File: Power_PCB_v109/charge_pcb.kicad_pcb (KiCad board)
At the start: 2 copper layers, 128.1 x 64 mm, 79 parts, among them J1 Mow3, J10 Mot_Left, J11 DC/DC1, J12 DC/DC2, J2 Main_PCB1, J3 Mow2, J4 Battery, J5 Main_PCB2, J6 Power Switch, J7 Mow1, J8 Mot_Right, J9 Start, Q1 BC547C, Q2 IRF9540N, Q3 BC547C, Q4 IRF9540N, U1 INA226, U2 INA226, U3 INA Charge, U4 INA226, U5 INA226, U6 INA226

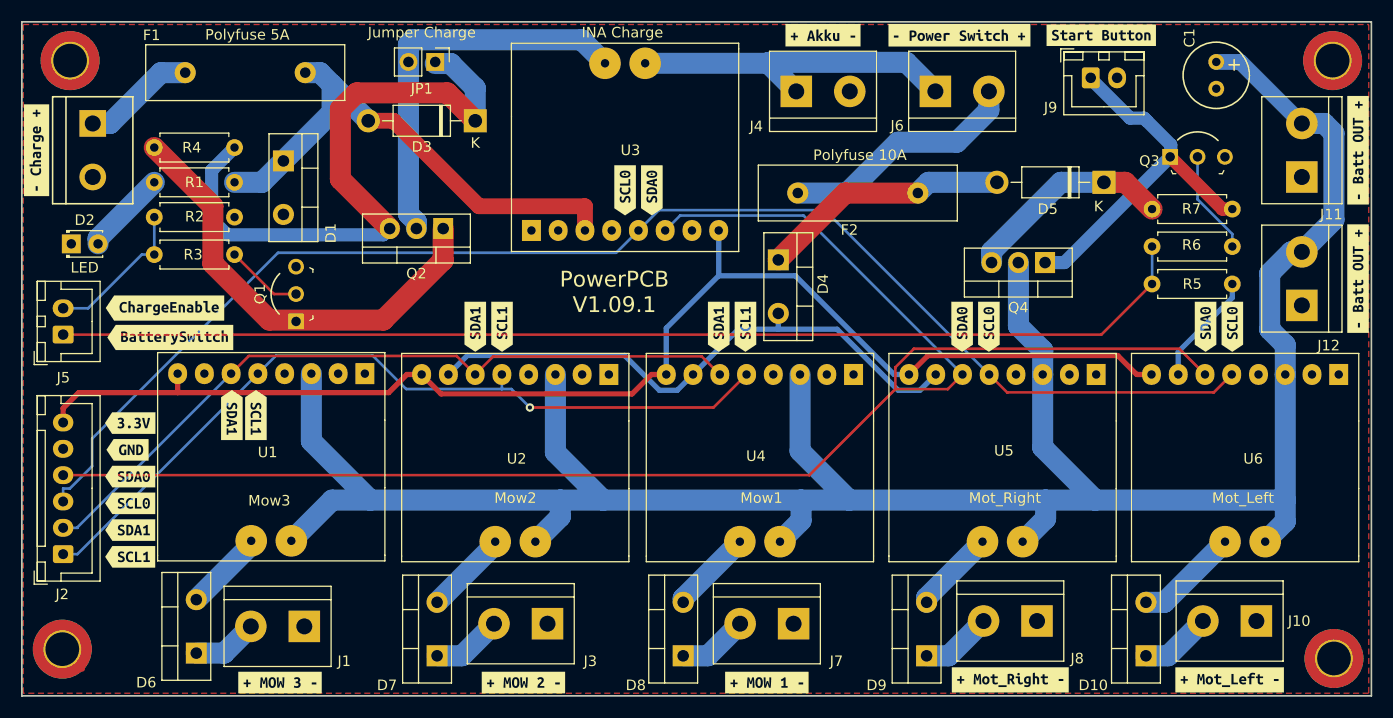
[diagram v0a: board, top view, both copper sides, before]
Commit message: Change SDA SCL Footprint
Ad new Schematic PDF and BOOM File
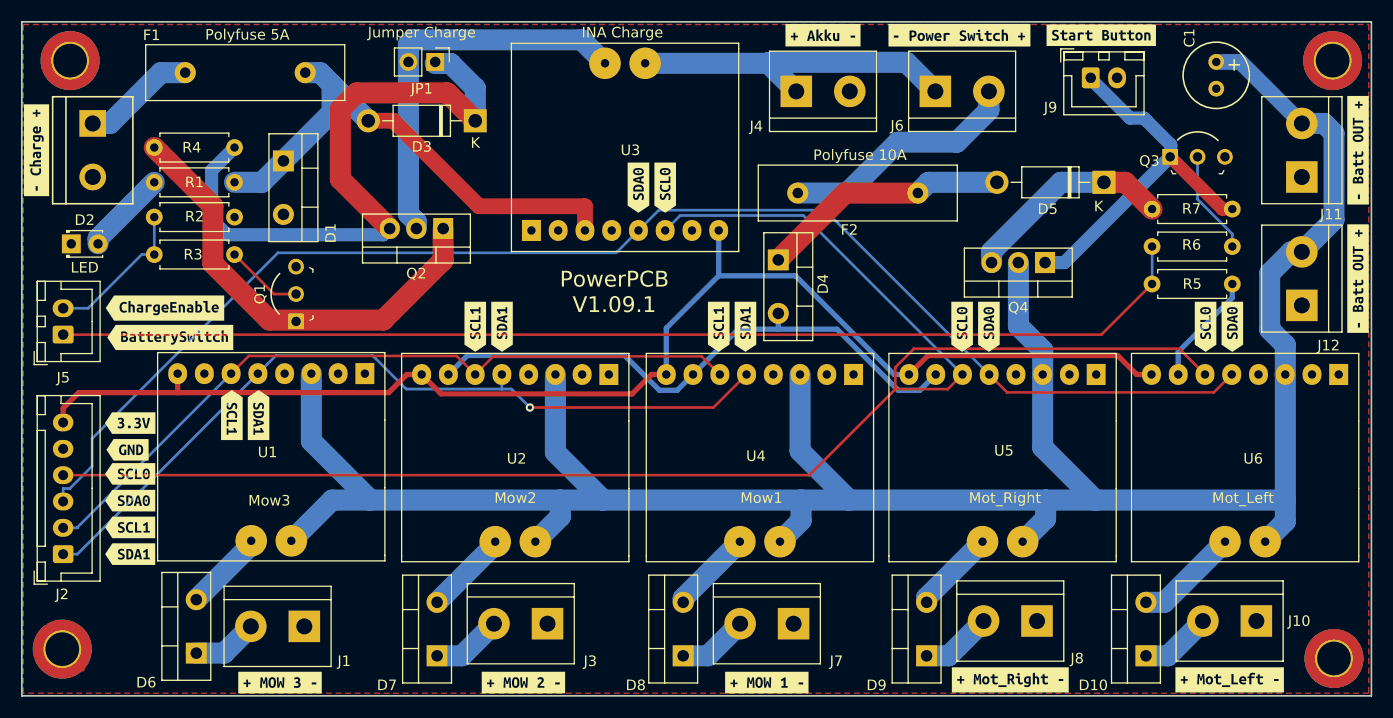
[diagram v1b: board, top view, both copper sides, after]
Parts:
- moved kibuzzard-6311B799 3.82 mm to (145.8, 77.0)
- moved kibuzzard-630F6337 2.79 mm to (95.0, 109.2)
- moved kibuzzard-630F68E0 2.79 mm to (95.0, 104.1)
- moved kibuzzard-6311B724 2.54 mm to (107.2, 98.6)
- moved kibuzzard-630FA50E 2.54 mm to (199.6, 90.2)
- moved kibuzzard-630FA52F 2.54 mm to (197.1, 90.2)
- moved kibuzzard-630FA55C 2.54 mm to (174.0, 90.2)
- moved kibuzzard-630FA573 2.54 mm to (176.5, 90.2)
- moved kibuzzard-630FA596 2.54 mm to (153.4, 90.2)
- moved kibuzzard-630FA5B5 2.54 mm to (150.9, 90.2)
- moved kibuzzard-630FA5E0 2.54 mm to (127.8, 90.2)
- moved kibuzzard-630FA5FF 2.54 mm to (130.3, 90.2)
- moved kibuzzard-630F6348 2.29 mm to (95.0, 111.8)
- moved kibuzzard-630F6901 2.29 mm to (95.0, 106.7)
- moved kibuzzard-6311B760 2.29 mm to (104.6, 98.6)
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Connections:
- J2 pad 1: SCL1 -> SDA1
- J2 pad 2: SDA1 -> SCL1
- J2 pad 3: SCL0 -> SDA0
- J2 pad 4: SDA0 -> SCL0
- U1 pad 5: SCL1 -> SDA1
- U1 pad 6: SDA1 -> SCL1
- U2 pad 5: SCL1 -> SDA1
- U2 pad 6: SDA1 -> SCL1
- U3 pad 5: SCL0 -> SDA0
- U3 pad 6: SDA0 -> SCL0
- U4 pad 5: SCL1 -> SDA1
- U4 pad 6: SDA1 -> SCL1
- U5 pad 5: SCL0 -> SDA0
- U5 pad 6: SDA0 -> SCL0
- U6 pad 5: SCL0 -> SDA0
- U6 pad 6: SDA0 -> SCL0
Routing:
- net SDA0: track 157.6 -> 132.5 mm
- net SCL0: track 132.5 -> 157.6 mm
- net SDA1: track 71.3 -> 77.4 mm, vias 0 -> 1
- net SCL1: track 77.4 -> 71.3 mm, vias 1 -> 0
